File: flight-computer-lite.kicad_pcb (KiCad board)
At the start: 2 copper layers, 65 x 65 mm, 89 parts, among them J1 USB_C_Receptacle_USB2.0_16P, J2 Micro_SD_Card_Det2, J3 Conn_01x02_Pin, J4 Conn_01x03_Pin, Q1 BSS138, SW1 SW_Push, SW2 SW_Push, U1 RP2040, U11 LM66200DRLR, U12 MAX-M10S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

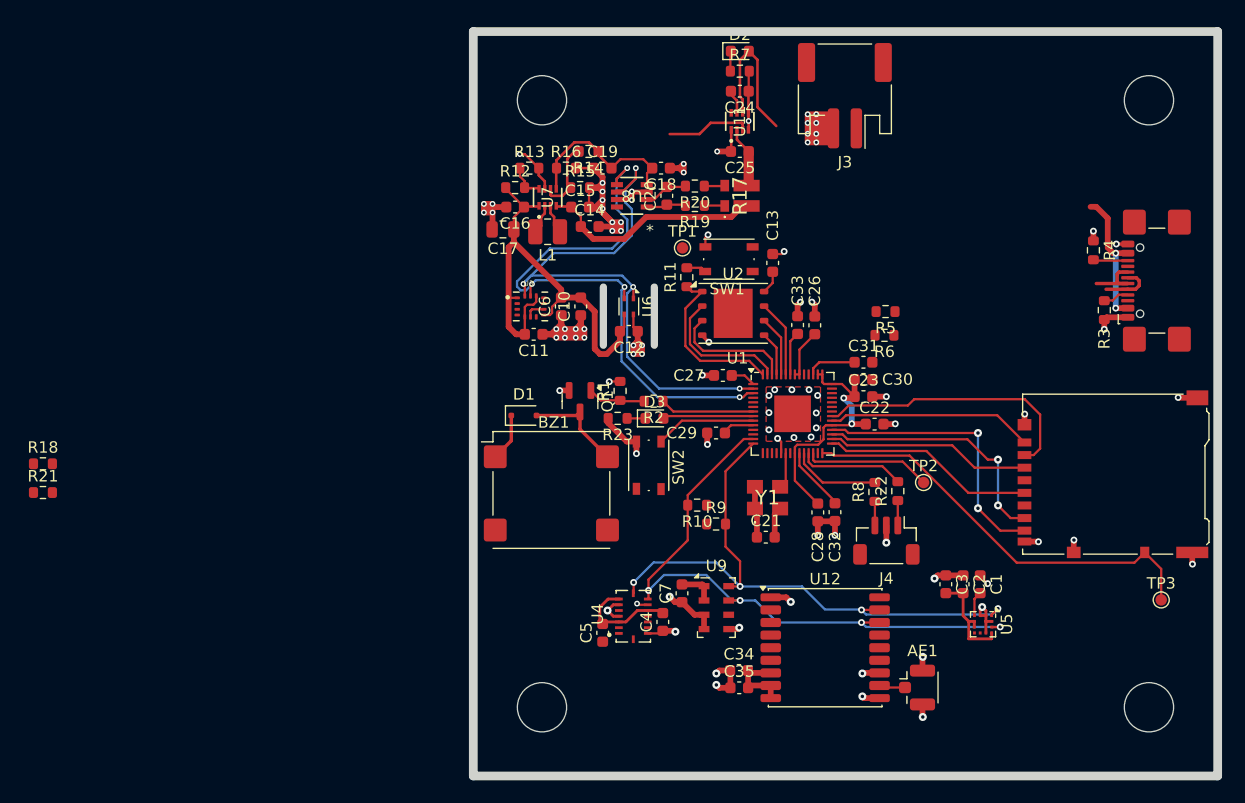
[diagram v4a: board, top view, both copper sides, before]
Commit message: Fixed PSU, routed
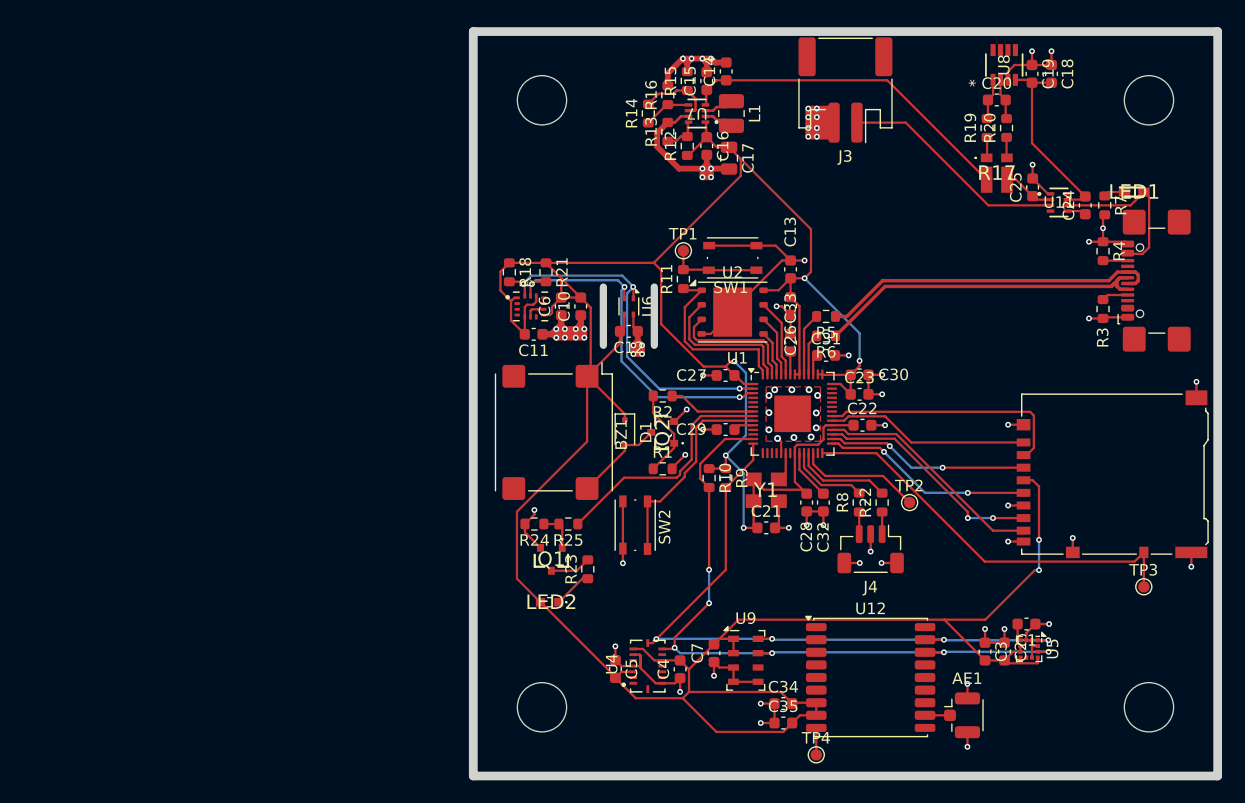
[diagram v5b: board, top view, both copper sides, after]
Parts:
- removed D2, D3: LED, LED_SMD:LED_0603_1608Metric
- added LED1: 150060VS55040, LRI_partlib:LEDM168X50N, F.Cu at (185.5, 66.8)
- added LED2: 150060SS55040, LRI_partlib:150060SS55040, F.Cu at (134.4, 102.6)
- added Q2: NX3008NBK,215, LRI_partlib:NX3008NBK215, F.Cu at (144.3, 87.8)
- added R24: 100K, Resistor_SMD:R_0603_1608Metric, F.Cu at (133.1, 95.8)
- added R25: 100R, Resistor_SMD:R_0603_1608Metric, F.Cu at (136.1, 95.8)
- added TP4: TestPoint, TestPoint:TestPoint_Pad_D1.0mm, F.Cu at (157.7, 115.9)
- Q1: value BSS138 -> NX3008NBK,215; footprint Package_TO_SOT_SMD:SOT-23 -> LRI_partlib:NX3008NBK215
- R12: value 107k -> 107K
- R13: value 19.1k -> 19.1K
- R23: value R -> 64.9R
- R7: value R -> 150R
- U5: footprint LRI_partlib:LGA-12_2x2mm_P0.5mm -> Package_LGA:LGA-12_2x2mm_P0.5mm
- U8: value SOT_32AIDDFR_TEX -> INA232AIDDFR
- moved R21 47.9 mm to (134.1, 73.8), turned to -90 degrees
- moved R18 44.0 mm to (130.9, 73.8), turned to -90 degrees
- moved C19 38.4 mm to (176.5, 56.4), turned to -90 degrees
- moved C18 35.1 mm to (178.2, 56.4), turned to -90 degrees
- moved U8 34.5 mm to (174.1, 55.7), turned to 90 degrees
- moved R7 34.0 mm to (182.9, 67.9), turned to -90 degrees
- moved C24 31.8 mm to (181.2, 67.9), turned to 90 degrees
- moved C20 30.0 mm to (173.5, 58.7), turned to 0 degrees
- moved U11 28.8 mm to (178.9, 67.7), turned to 0 degrees
- moved R20 27.7 mm to (174.3, 61.2), turned to 90 degrees
- moved R19 26.4 mm to (172.6, 61.2), turned to 90 degrees
- moved C25 25.8 mm to (176.6, 66.3), turned to 90 degrees
- moved R17 22.5 mm to (173.5, 65.1), turned to 0 degrees
- moved C17 20.7 mm to (150.1, 63.8), turned to -90 degrees
- moved L1 19.1 mm to (150.3, 59.9), turned to -90 degrees
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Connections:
- net /SC renamed Net-(U1-SWCLK)
- net /SD renamed Net-(U1-SWD)
- AE1 pad 2: GND -> (no net)
- Q1 pad 3: Net-(BZ1--) -> Net-(Q1-D)
- R1 pad 1: Net-(Q1-G) -> Net-(Q2-G)
- R14 pad 1: /PSU/+IN -> /PSU/-IN
- R14 pad 2: Net-(U7-MODE) -> /PSU/PIN6
- R15 pad 1: Net-(U7-MODE) -> /PSU/PIN6
- R16 pad 1: /PSU/+IN -> /PSU/-IN
- R2 pad 2: Net-(Q1-G) -> Net-(Q2-G)
- R23 pad 2: GND -> Net-(Q1-D)
- U12 pad 9: +3V3 -> Net-(U12-~{RESET})
- U2 pad 9: unconnected-(U2-EP-Pad9) -> GND
- U7 pad 5: /PSU/+IN -> /PSU/TPS_FB
- U7 pad 6: Net-(U7-MODE) -> GND
- U7 pad 7: GND -> /PSU/PIN6
- U7 pad 8: /PSU/TPS_FB -> /PSU/-IN
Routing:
- net +3V3: track 117.2 -> 310.9 mm, vias 2 -> 7
- net GND: track 118.0 -> 158.8 mm, vias 89 -> 80
- net /USB_D-: track 4.57 -> 30.2 mm
- net /USB_D+: track 5.42 -> 29.7 mm
- net /I2C Bus 1/I2C_1_SCL: track 51.9 -> 31.5 mm, vias 4 -> 3
- net /I2C Bus 1/I2C_1_SDA: track 51.8 -> 32.2 mm, vias 4 -> 3
- net /PSU/-IN: track 19.5 -> 33.9 mm
- net /USR_LED: track 7.92 -> 21.1 mm
- net +BATT: track 7.41 -> 19.9 mm
- net VBUS: track 26.0 -> 14.8 mm, vias 2 -> 0
- net /USR_BTN: track 8.81 -> 18.2 mm
- net Net-(Q2-G): track 0.00 -> 7.87 mm
- net Net-(U7-MODE): track 6.63 -> 0.00 mm
- net /PSU/PIN6: track 0.00 -> 6.58 mm
- net /I2C Bus 2/I2C_2_SCL: track 53.0 -> 59.6 mm
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
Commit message: Almost done with routing
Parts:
- removed the G*** at (160.2, 85.2)
- added G***: LOGO, LRI_partlib:rocket_miku_2, B.Cu at (161.9, 84.5)
- U8: value INA232AIDDFR -> SOT_32AIDDFR_TEX
- moved TP1 0.14 mm to (146.1, 71.8)
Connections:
- AE1 pad 2: (no net) -> GND
- J4 pad MP: (no net) -> GND
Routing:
- net /I2C Bus 1/I2C_1_SDA: track 32.2 -> 73.4 mm, vias 3 -> 4
- net /I2C Bus 1/I2C_1_SCL: track 31.5 -> 72.5 mm, vias 3 -> 5
- net +1V1: track 8.22 -> 23.0 mm, vias 0 -> 2
- net +3V3: track 310.9 -> 317.1 mm
- net GND: track 158.8 -> 160.2 mm, vias 80 -> 84

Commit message: Silkscreen finished
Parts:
- added G***: LOGO, LRI_partlib:oshpark-text, B.Cu at (147.3, 58.8)
- U8: value SOT_32AIDDFR_TEX -> INA232AIDDFR
- moved G*** 1.31 mm to (160.6, 85.0)
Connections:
- AE1 pad 2: GND -> (no net)
- J4 pad MP: GND -> (no net)
- R14 pad 2: /PSU/PIN6 -> Net-(U7-MODE)
- R15 pad 1: /PSU/PIN6 -> Net-(U7-MODE)
- U7 pad 5: /PSU/TPS_FB -> /PSU/-IN
- U7 pad 6: GND -> Net-(U7-MODE)
- U7 pad 7: /PSU/PIN6 -> GND
- U7 pad 8: /PSU/-IN -> /PSU/TPS_FB
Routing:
- net Net-(U7-MODE): track 0.00 -> 6.81 mm
- net /PSU/PIN6: track 6.81 -> 0.00 mm
- net /I2C Bus 1/I2C_1_SCL: track 72.5 -> 76.2 mm
- net GND: track 160.2 -> 162.8 mm, vias 84 -> 86
- net /PSU/+IN: track 21.3 -> 22.8 mm
- net /I2C Bus 1/I2C_1_SDA: track 73.4 -> 74.1 mm
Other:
- board text added: "5.5V MAX!"
- board text added: "BOOTSEL"
- board text added: "USR"

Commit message: Fixed slots
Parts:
- moved C18 113.9 mm to (68.8, 25.0), turned to 90 degrees
- moved C3 112.6 mm to (64.7, 74.1)
- moved C31 112.6 mm to (50.8, 48.3)
- moved C33 112.6 mm to (47.7, 47.2)
- moved LED1 112.6 mm to (77.7, 34.0)
- moved R1 112.6 mm to (36.5, 58.2)
- moved R10 112.6 mm to (40.6, 59.0)
- moved R12 112.6 mm to (38.7, 30.0)
- moved R15 112.6 mm to (38.7, 24.3)
- moved R19 112.6 mm to (64.9, 28.4)
- moved R25 112.6 mm to (28.3, 63.0)
- moved R3 112.6 mm to (75.0, 44.2)
- moved R4 112.6 mm to (75.0, 39.2)
- moved TP3 112.6 mm to (78.5, 68.5)
- moved U2 112.6 mm to (42.6, 44.5)
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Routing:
- net GND: track 162.8 -> 218.3 mm, vias 86 -> 94
- net /PSU/+IN: track 22.8 -> 22.2 mm
